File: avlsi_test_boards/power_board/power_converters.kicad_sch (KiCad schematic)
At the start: 15 parts, among them U6 TLV1117LV18DCYR, U7 TLV75709PDBV, U8 TLV1117LV25DCYR, U9 TLV1117LV33DCYR

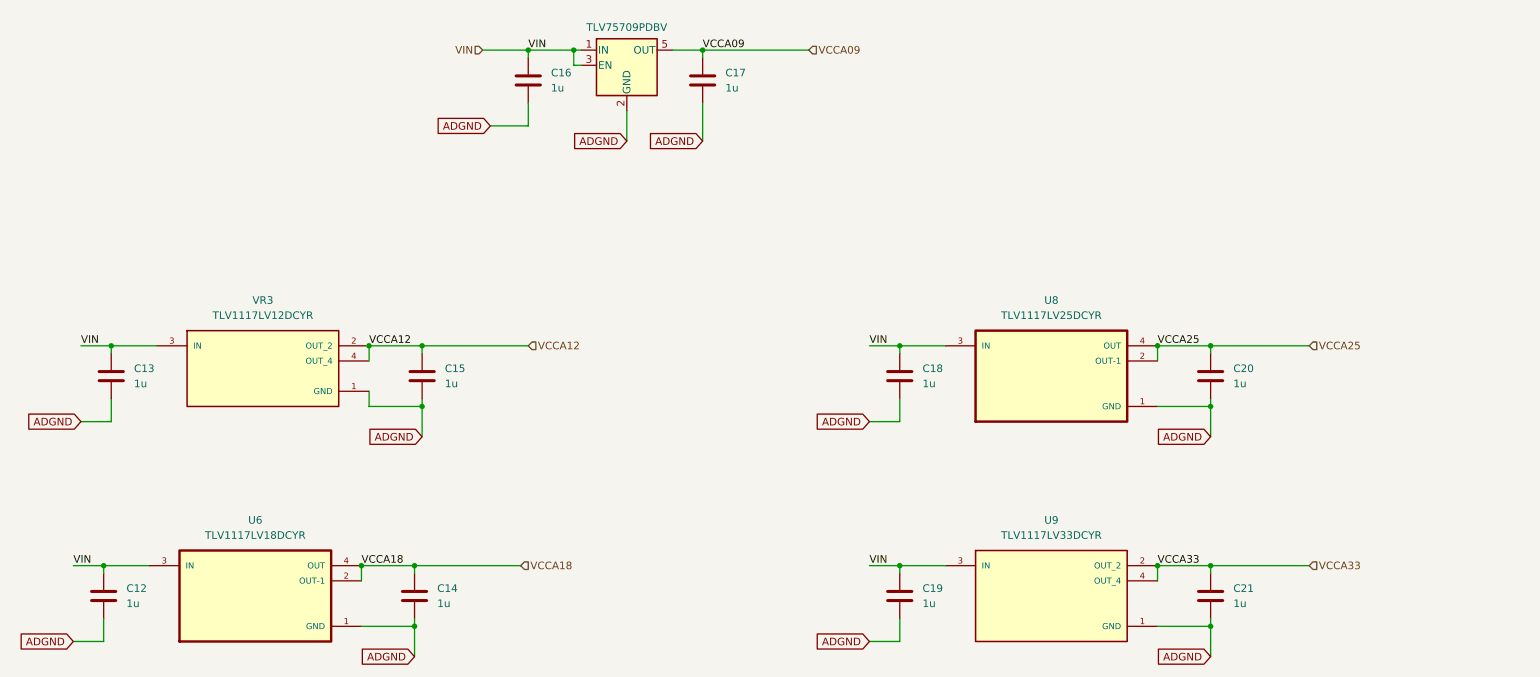
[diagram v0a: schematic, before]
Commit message: Add updated schematic
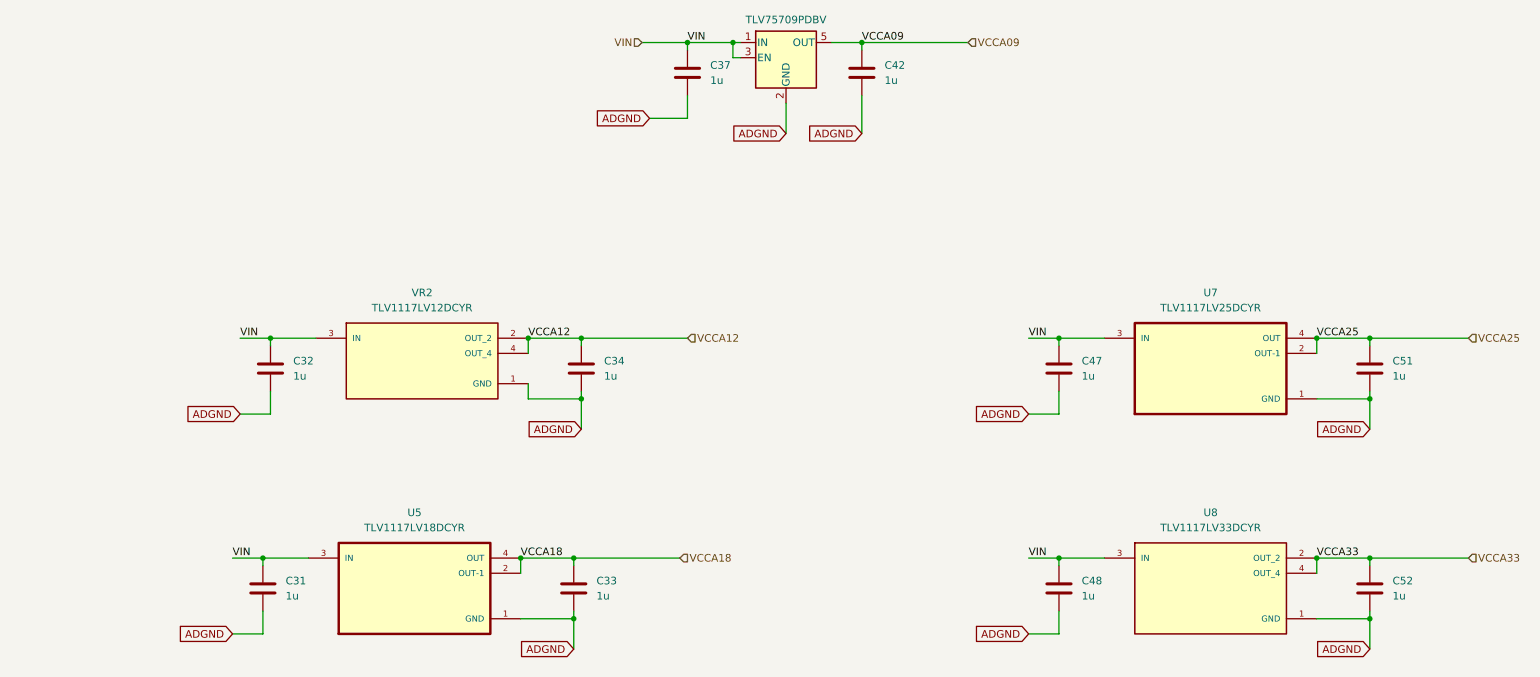
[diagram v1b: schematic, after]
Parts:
- renumbered C12 to C31, C13 to C32, C14 to C33, C15 to C34, C16 to C37, C17 to C42, C18 to C47, C19 to C48, C20 to C51, C21 to C52, U6 to U5, U7 to U6, U8 to U7, U9 to U8, VR3 to VR2
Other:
- moved on the sheet: C31, C32, C33, C34, C37, C42, C47, C48, C51, C52, U5, U7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
